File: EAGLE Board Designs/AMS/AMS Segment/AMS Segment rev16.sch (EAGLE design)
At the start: 145 parts, among them J0 CONNECTOR-1_5222_, J1 CONNECTOR-1_5222_, J10 CONNECTOR-1_5222_, J11 CONNECTOR-1_5222_, J12 CONNECTOR-1_5222_, J13 CONNECTOR-1_5222_, J14 CONNECTOR-1_5222_, J15 CONNECTOR-1_5222_, J16 CONNECTOR-1_5222_, J17 CONNECTOR-1_5222_, J18 CONNECTOR-1_5222_, J2 CONNECTOR-1_5222_, J27 CONNECTOR-2_MICROFIT_SMD_RIGH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, J28 CONNECTOR-2_MICROFIT_SMD_RIGH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, J29 CONNECTOR-1_5222_, J3 CONNECTOR-1_5222_, J30 CONNECTOR-1_5222_, J31 CONNECTOR-1_5222_, J32 CONNECTOR-2_MICROFIT_SMD_RIGH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, J33 CONNECTOR-2_MICROFIT_SMD_RIGH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, J34 CONNECTOR-2_MICROFIT_SMD_RIGH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, J35 CONNECTOR-2_MICROFIT_SMD_RIGH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, J37 CONNECTOR-2_MICROFIT_SMD_RIGH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, J38 CONNECTOR-2_MICROFIT_SMD_RIGH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, J39 CONNECTOR-2_MICROFIT_SMD_RIGH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, J4 CONNECTOR-1_5222_, J40 CONNECTOR-2_MICROFIT_SMD_RIGH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, J5 CONNECTOR-1_5222_, J6 CONNECTOR-1_5222_, J7 CONNECTOR-1_5222_, J8 CONNECTOR-1_5222_, J9 CONNECTOR-1_5222_, Q1 TRANSISTOR_NPN, Q2 TRANSISTOR_NPN, T1 TRANSFORMER_HM2112ZNLT, U1 LTC6811-2, U2 LTC6811-2, U3 SHT31-ARP-B, U4 SHT31-ARP-B

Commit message: AMS schematic approved
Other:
- moved on the sheet: C26, C28, C5, C6, J34, J35, R4, R49, R5, R50, R52, R6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

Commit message: Fixed ERC errors
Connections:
- removed net V+: C27.1, R44.2, U1.V+
- removed net V+B: C13.1, R24.1, U2.V+
- removed net V-B: C10.2, C11.2, C15.2, C16.2, C17.2, C26.1, C4.2, C9.2, R10.1, R12.1
- removed net V-_L: C7.2, R29.1, U2.V-
- removed net V-_U: C14.2, R27.1, U1.V-
- removed net VREF2L: C1.1, C24.1, U2.VREF2, U4.VDD
- removed net VREF2U: C25.1, C4.1, U1.VREF2, U3.VDD
- new net VREFL: C1.1, U2.VREF2
- net V+L: now also C13.1, R24.1, U2.V+
- net V+U: now also C27.1, R44.2, U1.V+
- net V-: no longer C12.2, C13.2, C2.2, C20.2, C21.2, C22.2, C23.2, C28.1, C3.2, R18.1, R20.1
- net V-L: now also C1.2, C12.2, C13.2, C2.2, C20.2, C21.2, C22.2, C23.2, C28.1, C3.2, C7.2, R18.1, R20.1, R29.1, U2.V-
- net V-U: now also C10.2, C11.2, C14.2, C15.2, C16.2, C17.2, C26.1, C4.2, C9.2, R10.1, R12.1, R27.1, U1.V-
- net VREGL: now also C24.1, U4.VDD
- net VREGU: now also C25.1, C4.1, U1.VREF2, U3.VDD

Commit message: Revert "holder push"
This reverts commit 5c5a8d45b60ff0506a7db83585d04c86d1c2f773.
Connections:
- removed net VREFL: C1.1, U2.VREF2
- new net V+: C27.1, R44.2, U1.V+
- new net V+B: C13.1, R24.1, U2.V+
- new net V-B: C10.2, C11.2, C15.2, C16.2, C17.2, C26.1, C4.2, C9.2, R10.1, R12.1
- new net V-_L: C7.2, R29.1, U2.V-
- new net V-_U: C14.2, R27.1, U1.V-
- new net VREF2L: C1.1, C24.1, U2.VREF2, U4.VDD
- new net VREF2U: C25.1, C4.1, U1.VREF2, U3.VDD
- net V+L: no longer C13.1, R24.1, U2.V+
- net V+U: no longer C27.1, R44.2, U1.V+
- net V-: now also C12.2, C13.2, C2.2, C20.2, C21.2, C22.2, C23.2, C28.1, C3.2, R18.1, R20.1
- net V-L: no longer C1.2, C12.2, C13.2, C2.2, C20.2, C21.2, C22.2, C23.2, C28.1, C3.2, C7.2, R18.1, R20.1, R29.1, U2.V-
- net V-U: no longer C10.2, C11.2, C14.2, C15.2, C16.2, C17.2, C26.1, C4.2, C9.2, R10.1, R12.1, R27.1, U1.V-
- net VREGL: no longer C24.1, U4.VDD
- net VREGU: no longer C25.1, C4.1, U1.VREF2, U3.VDD

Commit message: Fixed erc errors again
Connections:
- removed net V+: C27.1, R44.2, U1.V+
- removed net V+B: C13.1, R24.1, U2.V+
- removed net V-B: C10.2, C11.2, C15.2, C16.2, C17.2, C26.1, C4.2, C9.2, R10.1, R12.1
- removed net V-_L: C7.2, R29.1, U2.V-
- removed net V-_U: C14.2, R27.1, U1.V-
- removed net VREF2L: C1.1, C24.1, U2.VREF2, U4.VDD
- net V+L: now also C13.1, R24.1, U2.V+
- net V+U: now also C27.1, R44.2, U1.V+
- net V-: no longer C12.2, C13.2, C2.2, C20.2, C21.2, C22.2, C23.2, C28.1, C3.2, R18.1, R20.1
- net V-L: now also C1.2, C12.2, C13.2, C2.2, C20.2, C21.2, C22.2, C23.2, C28.1, C3.2, C7.2, R18.1, R20.1, R29.1, U2.V-
- net V-U: now also C10.2, C11.2, C14.2, C15.2, C16.2, C17.2, C26.1, C4.2, C9.2, R10.1, R12.1, R27.1, U1.V-
- net VREF2U: no longer C25.1, U3.VDD
- net VREGL: now also C1.1, C24.1, U2.VREF2, U4.VDD
- net VREGU: now also C25.1, U3.VDD

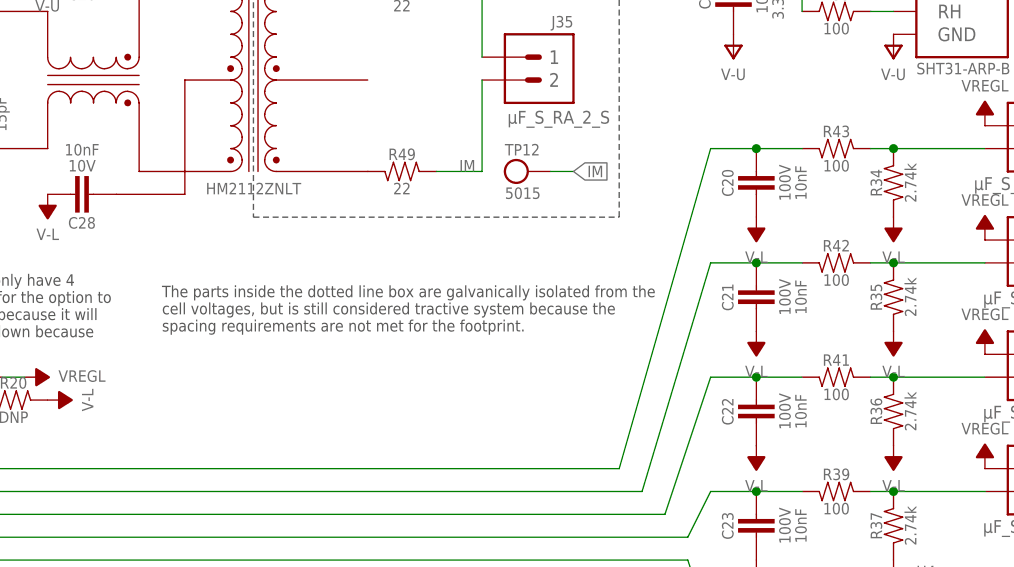
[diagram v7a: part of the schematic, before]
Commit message: Added note about EV.8.3.2
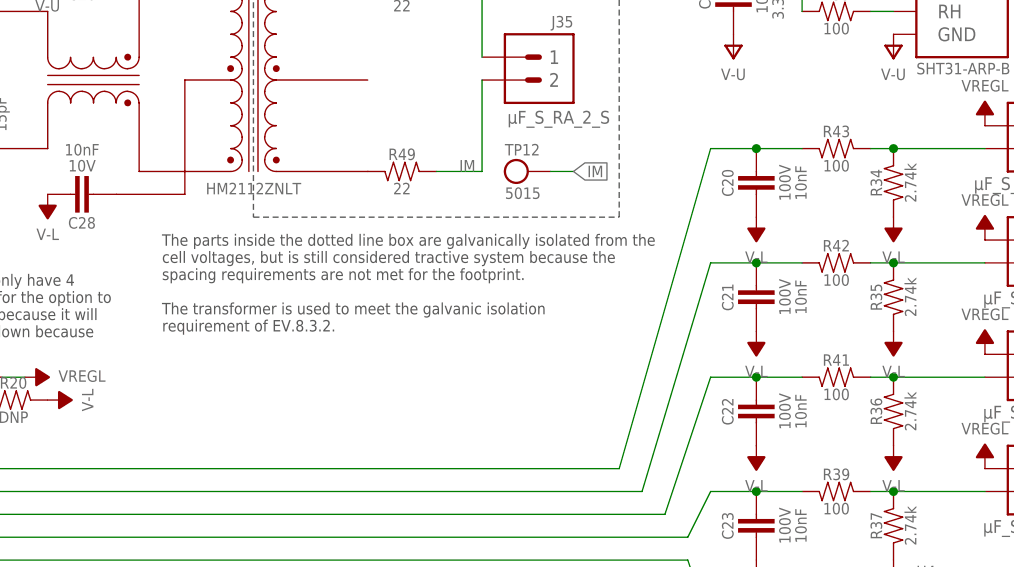
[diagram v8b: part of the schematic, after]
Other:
- note added: "The parts inside the dotted line box are galvanically isolated from the cell voltages, but is still considered tractive system because the spacing requirements are not met for the footprint. The transformer is used to meet the galvanic isolation requirement of EV.8.3.2."
- note removed: "The parts inside the dotted line box are galvanically isolated from the cell voltages, but is still considered tractive system because the spacing requirements are not met for the footprint."
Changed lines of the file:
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@@
 <text x="172.72" y="104.14" size="1.27" layer="97">The parts inside the dotted line box are galvanically isolated from the
 cell voltages, but is still considered tractive system because the
-spacing requirements are not met for the footprint.</text>
+spacing requirements are not met for the footprint.
+The transformer is used to meet the galvanic isolation
+requirement of EV.8.3.2.</text>
 </plain>
 <moduleinsts>
